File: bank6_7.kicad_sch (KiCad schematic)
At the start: 1 part, among them U1 ECP5-BGA256

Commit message: schematic wip
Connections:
- net +3V3: no longer U1.L4 (PL29C), U1.M4 (PL35C), U1.M5 (PL44C), U1.N5 (PL44D), U1.P4 (PL41A), U1.R5 (PL44A)
- net GND: no longer U1.L3 (PL32C), U1.M3 (PL32D), U1.N6 (PL47B), U1.P5 (PL47D), U1.P6 (PL47C)
- net MEZZANINE18: now reaches U1.K4 (PL29A)
- net MEZZANINE19: now reaches U1.K5 (PL29B)
- net MEZZANINE20: now reaches U1.L1 (PL26A)
- net MEZZANINE21: now reaches U1.L2 (PL26B)
- net MEZZANINE9: now reaches U1.M1 (PL26C)
- net MEZZANINE8: now reaches U1.M2 (PL26D)
- net MEZZANINE10: now reaches U1.N1 (PL32A)
- net MEZZANINE6: now reaches U1.N3 (PL35D)
- net MEZZANINE24: now reaches U1.N4 (PL38A)
- net MEZZANINE3: now reaches U1.P1 (PL35A)
- net MEZZANINE13: now reaches U1.P2 (PL32B)
- net MEZZANINE22: now reaches U1.P3 (PL38B)
- net MEZZANINE4: now reaches U1.R1 (PL35B)
- net MEZZANINE5: now reaches U1.R2 (PL38C)
- net MEZZANINE26: now reaches U1.R3 (PL41B)
- net MEZZANINE27: now reaches U1.R4 (PL41C)
- net MEZZANINE7: now reaches U1.T2 (PL38D)
- net MEZZANINE23: now reaches U1.T3 (PL41D)
- net MEZZANINE28: now reaches U1.T4 (PL44B)
- net ~{BTN_USER}: now reaches U1.G1 (PL20A)
- net VCCRAM renamed +1V8
- new net MEZZANINE11: U1.L4 (PL29C)
- new net MEZZANINE12: U1.L3 (PL32C)
- new net MEZZANINE25: U1.M3 (PL32D)
- new net PMOD1: U1.M4 (PL35C)
- new net PMOD10: U1.P6 (PL47C)
- new net PMOD2: U1.R5 (PL44A)
- new net PMOD3: U1.M5 (PL44C)
- new net PMOD4: U1.N5 (PL44D)
- new net PMOD7: U1.P4 (PL41A)
- new net PMOD8: U1.N6 (PL47B)
- new net PMOD9: U1.P5 (PL47D)
- no-connect marks 24 -> 4

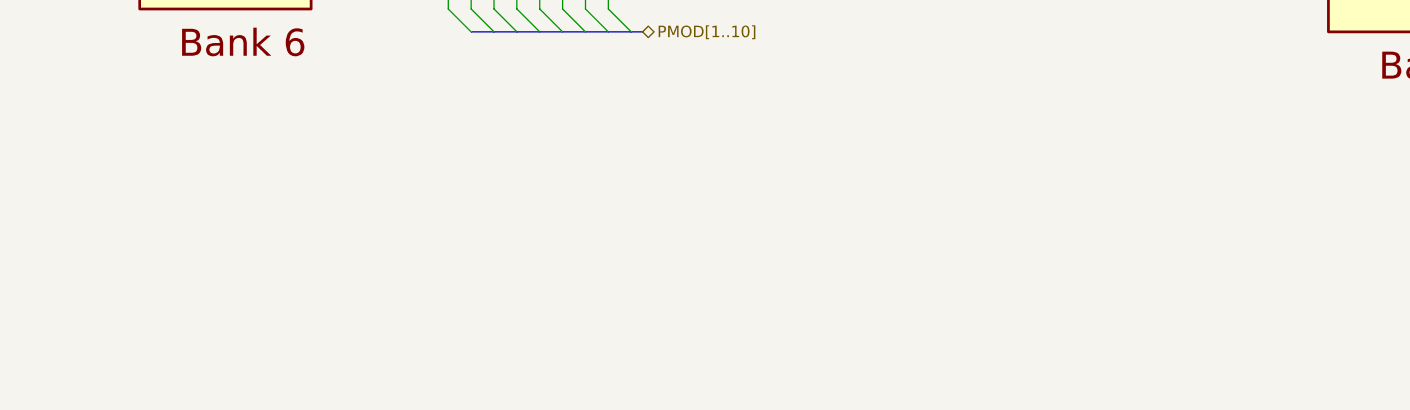
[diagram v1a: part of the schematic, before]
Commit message: add regulator for analog 3.3 V supply
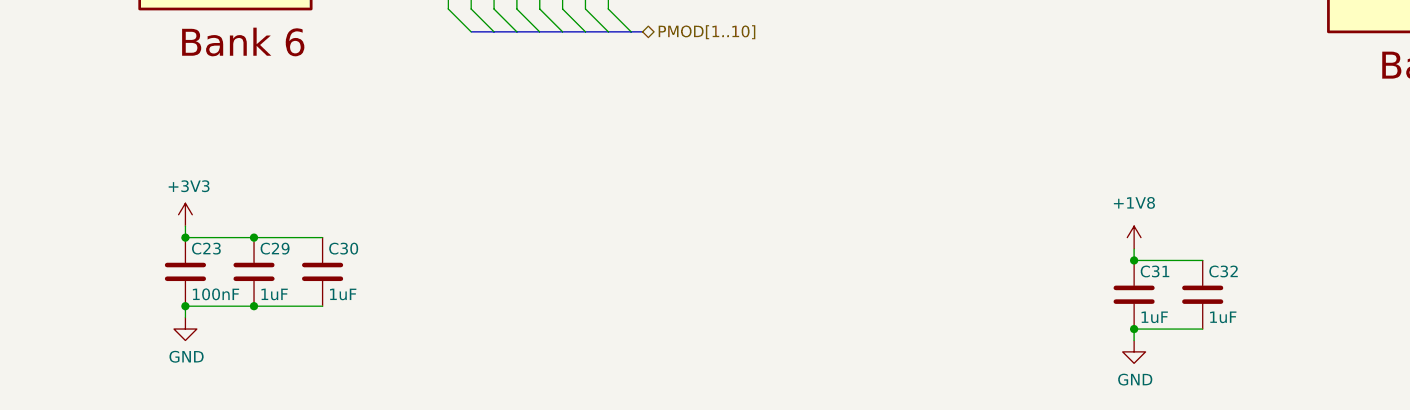
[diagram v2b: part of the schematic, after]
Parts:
- added C23: 100nF, Capacitor_SMD:C_0402_1005Metric, symbol Device:C
- added C29, C30, C31, C32: 1uF, Capacitor_SMD:C_0402_1005Metric, symbol Device:C
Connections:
- net +1V8: now also C31.1, C32.1
- net +3V3: now also C23.1, C29.1, C30.1
- net GND: now also C23.2, C29.2, C30.2, C31.2, C32.2

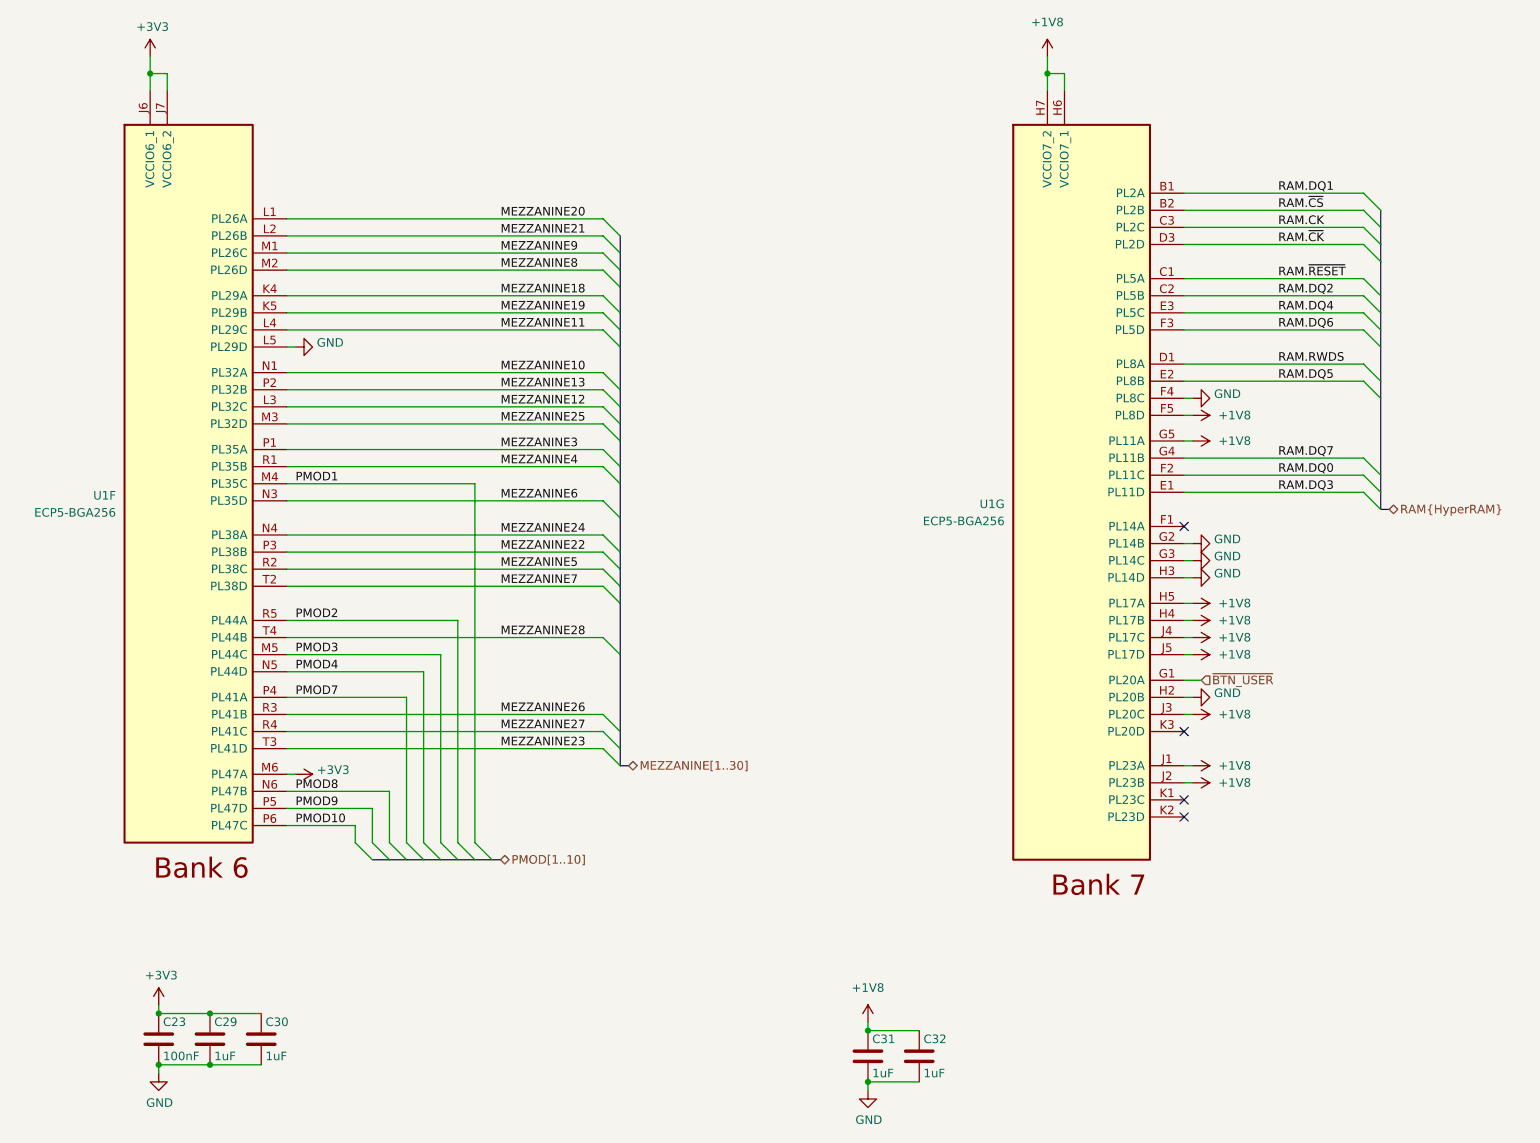
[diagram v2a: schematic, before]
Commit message: complete initial layout
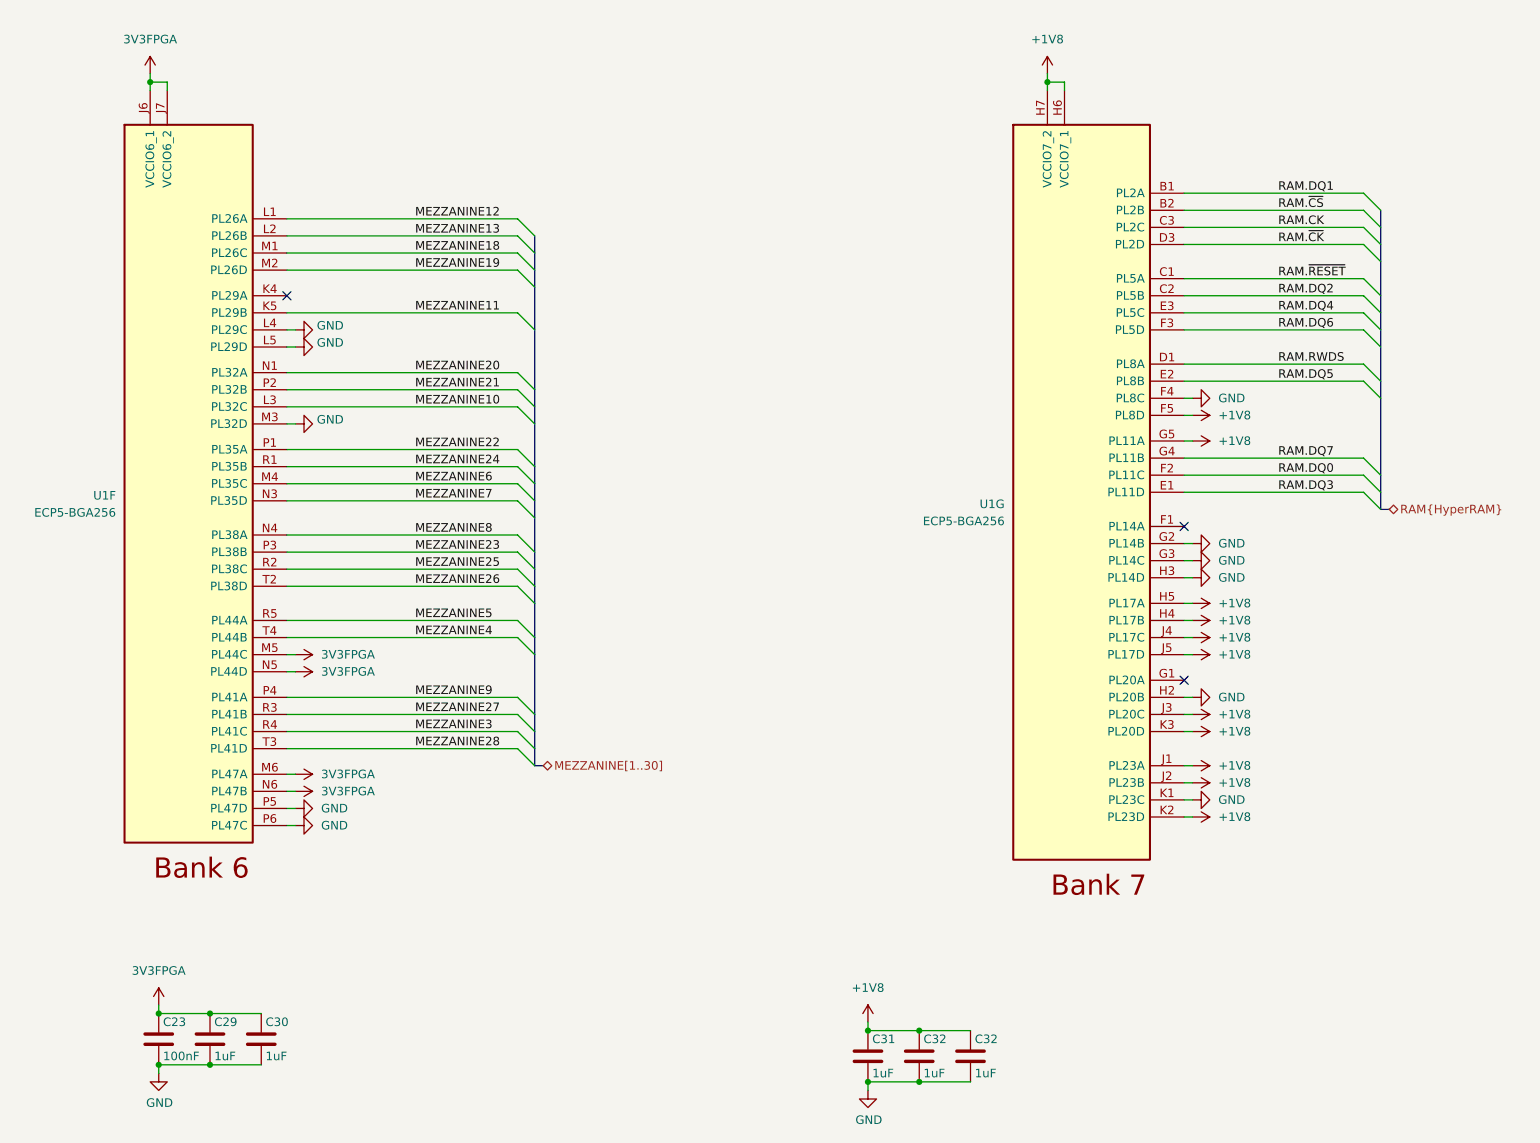
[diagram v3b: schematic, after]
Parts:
- added C32: 1uF, Capacitor_SMD:C_0402_1005Metric, symbol Device:C
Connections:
- net PMOD1 is gone; now on net MEZZANINE6: U1.M4 (PL35C)
- net PMOD10 is gone; now on net GND: U1.P6 (PL47C)
- net PMOD2 is gone; now on net MEZZANINE5: U1.R5 (PL44A)
- net PMOD3 is gone; now on net 3V3FPGA: U1.M5 (PL44C)
- net PMOD4 is gone; now on net 3V3FPGA: U1.N5 (PL44D)
- net PMOD7 is gone; now on net MEZZANINE9: U1.P4 (PL41A)
- net PMOD8 is gone; now on net 3V3FPGA: U1.N6 (PL47B)
- net PMOD9 is gone; now on net GND: U1.P5 (PL47D)
- net +1V8: now also U1.K2 (PL23D), U1.K3 (PL20D), C32.1
- net GND: now also U1.K1 (PL23C), U1.L4 (PL29C), U1.M3 (PL32D), C32.2
- net MEZZANINE10: now also U1.L3 (PL32C); no longer U1.N1 (PL32A)
- net MEZZANINE11: now also U1.K5 (PL29B); no longer U1.L4 (PL29C)
- net MEZZANINE12: now also U1.L1 (PL26A); no longer U1.L3 (PL32C)
- net MEZZANINE13: now also U1.L2 (PL26B); no longer U1.P2 (PL32B)
- net MEZZANINE18: now also U1.M1 (PL26C); no longer U1.K4 (PL29A)
- net MEZZANINE19: now also U1.M2 (PL26D); no longer U1.K5 (PL29B)
- net MEZZANINE20: now also U1.N1 (PL32A); no longer U1.L1 (PL26A)
- net MEZZANINE21: now also U1.P2 (PL32B); no longer U1.L2 (PL26B)
- net MEZZANINE22: now also U1.P1 (PL35A); no longer U1.P3 (PL38B)
- net MEZZANINE23: now also U1.P3 (PL38B); no longer U1.T3 (PL41D)
- net MEZZANINE24: now also U1.R1 (PL35B); no longer U1.N4 (PL38A)
- net MEZZANINE25: now also U1.R2 (PL38C); no longer U1.M3 (PL32D)
- net MEZZANINE26: now also U1.T2 (PL38D); no longer U1.R3 (PL41B)
- net MEZZANINE27: now also U1.R3 (PL41B); no longer U1.R4 (PL41C)
- net MEZZANINE28: now also U1.T3 (PL41D); no longer U1.T4 (PL44B)
- net MEZZANINE3: now also U1.R4 (PL41C); no longer U1.P1 (PL35A)
- net MEZZANINE4: now also U1.T4 (PL44B); no longer U1.R1 (PL35B)
- net MEZZANINE5: no longer U1.R2 (PL38C)
- net MEZZANINE6: no longer U1.N3 (PL35D)
- net MEZZANINE7: now also U1.N3 (PL35D); no longer U1.T2 (PL38D)
- net MEZZANINE8: now also U1.N4 (PL38A); no longer U1.M2 (PL26D)
- net MEZZANINE9: no longer U1.M1 (PL26C)
- net +3V3 renamed 3V3FPGA
- net ~{BTN_USER}: no longer names the net of U1.G1 (PL20A)
- no-connect marks 4 -> 3
